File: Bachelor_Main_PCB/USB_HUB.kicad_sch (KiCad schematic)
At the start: 16 parts, among them J11 M20-9990245, U6 USB2514B-I/M2, Y3 SG-210STF 24Mhz

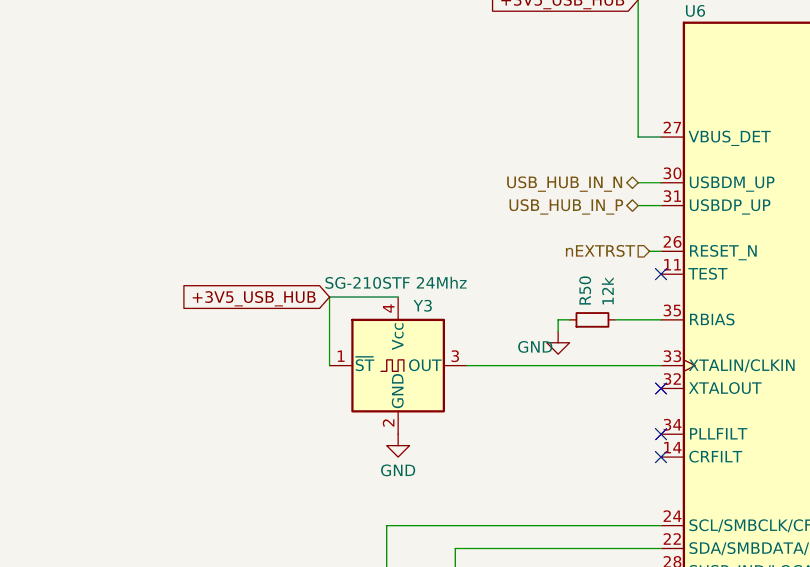
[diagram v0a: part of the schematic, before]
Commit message: Achematic review changes. Smal ones. Replaced TX_ON LED
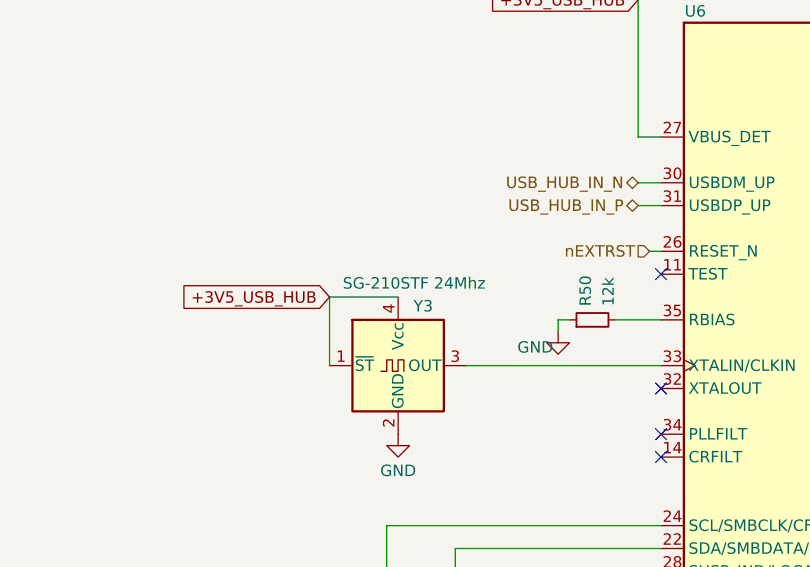
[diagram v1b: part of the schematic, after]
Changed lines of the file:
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@@
 		)
 		(property "Value" "SG-210STF 24Mhz"
-			(at 73.406 93.726 0)
+			(at 75.438 93.726 0)
 			(effects
 				(font

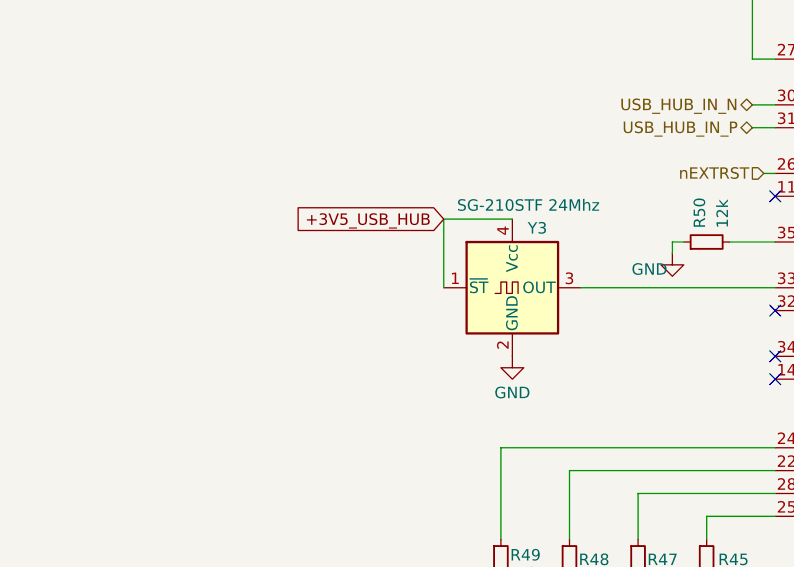
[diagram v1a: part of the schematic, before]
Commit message: added 100nF to 24Mhz oscillators
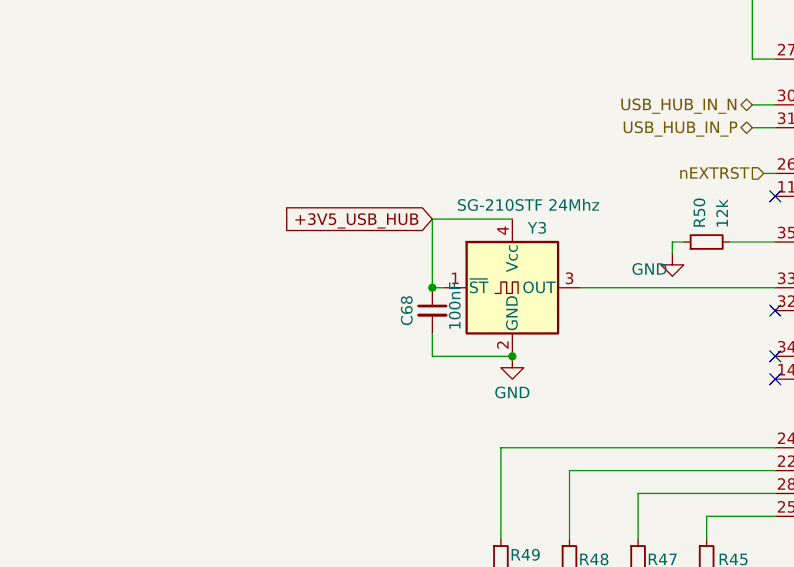
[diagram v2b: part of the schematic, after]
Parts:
- added C68: 100nF, Capacitor_SMD:C_0603_1608Metric, symbol Device:C_Small
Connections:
- net +3V5_USB_HUB: now also C68.1
- net GND: now also C68.2
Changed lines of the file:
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@@
+	)
+	(junction
+		(at 73.66 110.49)
+		(diameter 0)
+		(color 0 0 0 0)
 	)
 	(junction
@@
 	)
 	(junction
+		(at 64.77 102.87)
+		(diameter 0)
+		(color 0 0 0 0)
+	)
+	(junction
 		(at 148.59 182.88)
 		(diameter 0)
@@
 	(wire
 		(pts
+			(xy 64.77 110.49) (xy 73.66 110.49)
+		)
+		(stroke
+			(width 0)
+			(type default)
+		)
+	)
+	(wire
+		(pts
 			(xy 72.39 120.65) (xy 72.39 130.81)
 		)
@@
 	(wire
 		(pts
-			(xy 66.04 95.25) (xy 73.66 95.25)
+			(xy 64.77 95.25) (xy 73.66 95.25)
+		)
+		(stroke
+			(width 0)
+			(type default)
+		)
+	)
+	(wire
+		(pts
+			(xy 64.77 102.87) (xy 66.04 102.87)
 		)
 		(stroke
@@
 	(wire
 		(pts
-			(xy 66.04 102.87) (xy 66.04 95.25)
+			(xy 64.77 95.25) (xy 64.77 102.87)
 		)
 		(stroke
@@
 		(pts
 			(xy 133.35 182.88) (xy 140.97 182.88)
+		)
+		(stroke
+			(width 0)
+			(type default)
+		)
+	)
+	(wire
+		(pts
+			(xy 64.77 107.95) (xy 64.77 110.49)
 		)
 		(stroke
@@
 	(global_label "+3V5_USB_HUB"
 		(shape input)
-		(at 66.04 95.25 180)
+		(at 64.77 95.25 180)
 		(fields_autoplaced yes)
 		(effects
@@
 		)
 		(property "Intersheetrefs" "${INTERSHEET_REFS}"
-			(at 48.2986 95.25 0)
+			(at 47.0286 95.25 0)
 			(effects
 				(font
@@
 					(unit 1)
 				)
+			)
+		)
+	)
+	(symbol
+		(lib_id "Device:C_Small")
+		(at 64.77 105.41 0)
+		(unit 1)
+		(exclude_from_sim no)
+		(in_bom yes)
+		(on_board yes)
+		(dnp no)
+		(property "Reference" "C68"
+			(at 61.976 105.41 90)
+			(effects
+				(font
+					(size 1.27 1.27)
+				)
+			)
+		)
+		(property "Value" "100nF"
+			(at 67.31 104.902 90)
+			(effects
+				(font
+					(size 1.27 1.27)
+				)
+			)
+		)
+		(property "Footprint" "Capacitor_SMD:C_0603_1608Metric"
+			(at 64.77 105.41 0)
+			(effects
+				(font
+					(size 1.27 1.27)
+				)
+				(hide yes)
+			)
+		)
+		(property "Datasheet" "~"
+			(at 64.77 105.41 0)
+			(effects
+				(font
+					(size 1.27 1.27)
+				)
+				(hide yes)
+			)
+		)
+		(property "Description" "Unpolarized capacitor, small symbol"
+			(at 64.77 105.41 0)
+			(effects
+				(font
+					(size 1.27 1.27)
+				)
+				(hide yes)
+			)
+		)
+		(property "Field5" ""
+			(at 64.77 105.41 0)
+			(effects
+				(font
+					(size 1.27 1.27)
+				)
+				(hide yes)
+			)
+		)
+		(property "Field6" ""
+			(at 64.77 105.41 0)
+			(effects
+				(font
+					(size 1.27 1.27)
+				)
+				(hide yes)
+			)
+		)
+		(pin "2"
+		)
+		(pin "1"
+		)
+		(instances
+			(project "Bachelor_Main_PCB"
+				(path "/3544d663-329e-4884-b753-28436ca187e8/a2efe210-cbe4-4166-b2f4-897451b29d8a"
+					(reference "C68")
+					(unit 1)
+				)

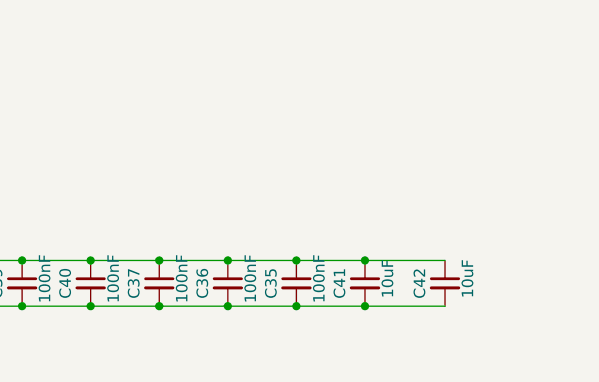
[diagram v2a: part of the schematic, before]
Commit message: Add correct 10uF partno
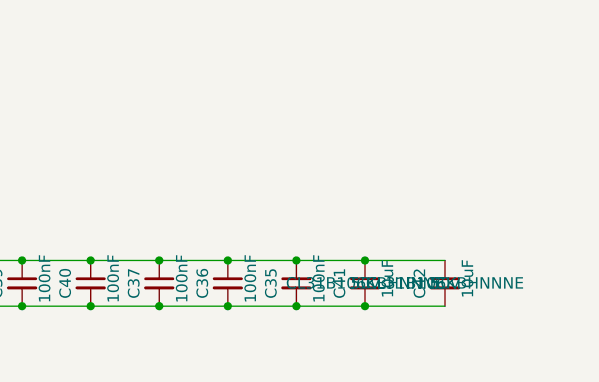
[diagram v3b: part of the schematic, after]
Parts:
- C41, C42: footprint Capacitor_SMD:C_0603_1608Metric -> Capacitor_SMD:C_1206_3216Metric; Part-no (none) -> CL31B106KBHNNNE; Voltage rating (none) -> 50v
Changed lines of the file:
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@@
 			)
 		)
-		(property "Footprint" "Capacitor_SMD:C_0603_1608Metric"
+		(property "Footprint" "Capacitor_SMD:C_1206_3216Metric"
 			(at 156.21 180.34 0)
 			(effects
@@
 				)
 				(hide yes)
+			)
+		)
+		(property "Part-no" "CL31B106KBHNNNE "
+			(at 156.21 180.34 0)
+			(effects
+				(font
+					(size 1.27 1.27)
+				)
+			)
+		)
+		(property "Voltage rating" "50v"
+			(at 156.21 180.34 0)
+			(effects
+				(font
+					(size 1.27 1.27)
+				)
 			)
 		)
@@
 			)
 		)
-		(property "Footprint" "Capacitor_SMD:C_0603_1608Metric"
+		(property "Footprint" "Capacitor_SMD:C_1206_3216Metric"
 			(at 165.1 180.34 0)
 			(effects
@@
 			)
 		)
+		(property "Part-no" "CL31B106KBHNNNE "
+			(at 165.1 180.34 0)
+			(effects
+				(font
+					(size 1.27 1.27)
+				)
+			)
+		)
+		(property "Voltage rating" "50v"
+			(at 165.1 180.34 0)
+			(effects
+				(font
+					(size 1.27 1.27)
+				)
+			)
+		)

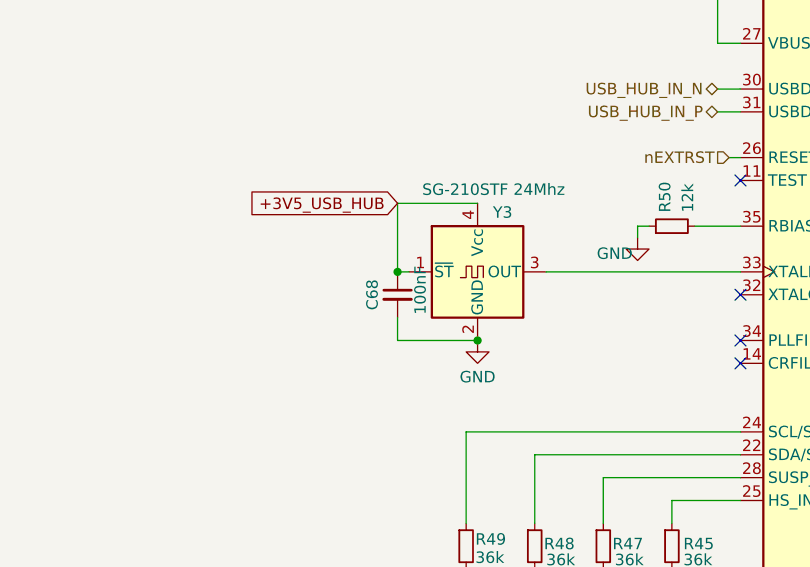
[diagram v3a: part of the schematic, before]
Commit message: Remove 24Mhz oscillators from hub and tranciever
Replaced with trace to PA8 pin which is the internaly supplied oscillator from the MCU
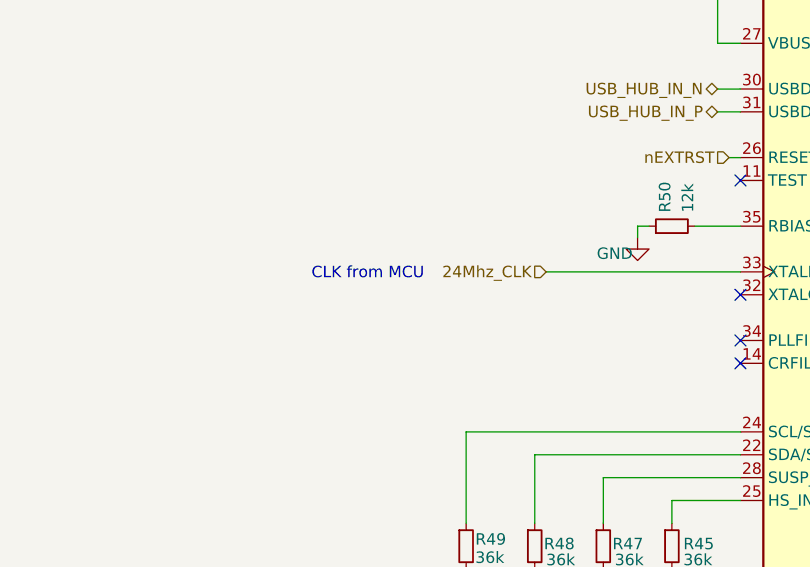
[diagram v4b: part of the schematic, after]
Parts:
- removed C68: 100nF, Capacitor_SMD:C_0603_1608Metric, symbol Device:C_Small
- removed Y3: SG-210STF 24Mhz, Oscillator:Oscillator_SMD_SeikoEpson_SG210-4Pin_2.5x2.0mm, symbol Oscillator:SG-210STF
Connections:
- net 24Mhz_CLK: now reaches U6.33 (XTALIN/CLKIN)
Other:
- note added: "CLK from MCU"

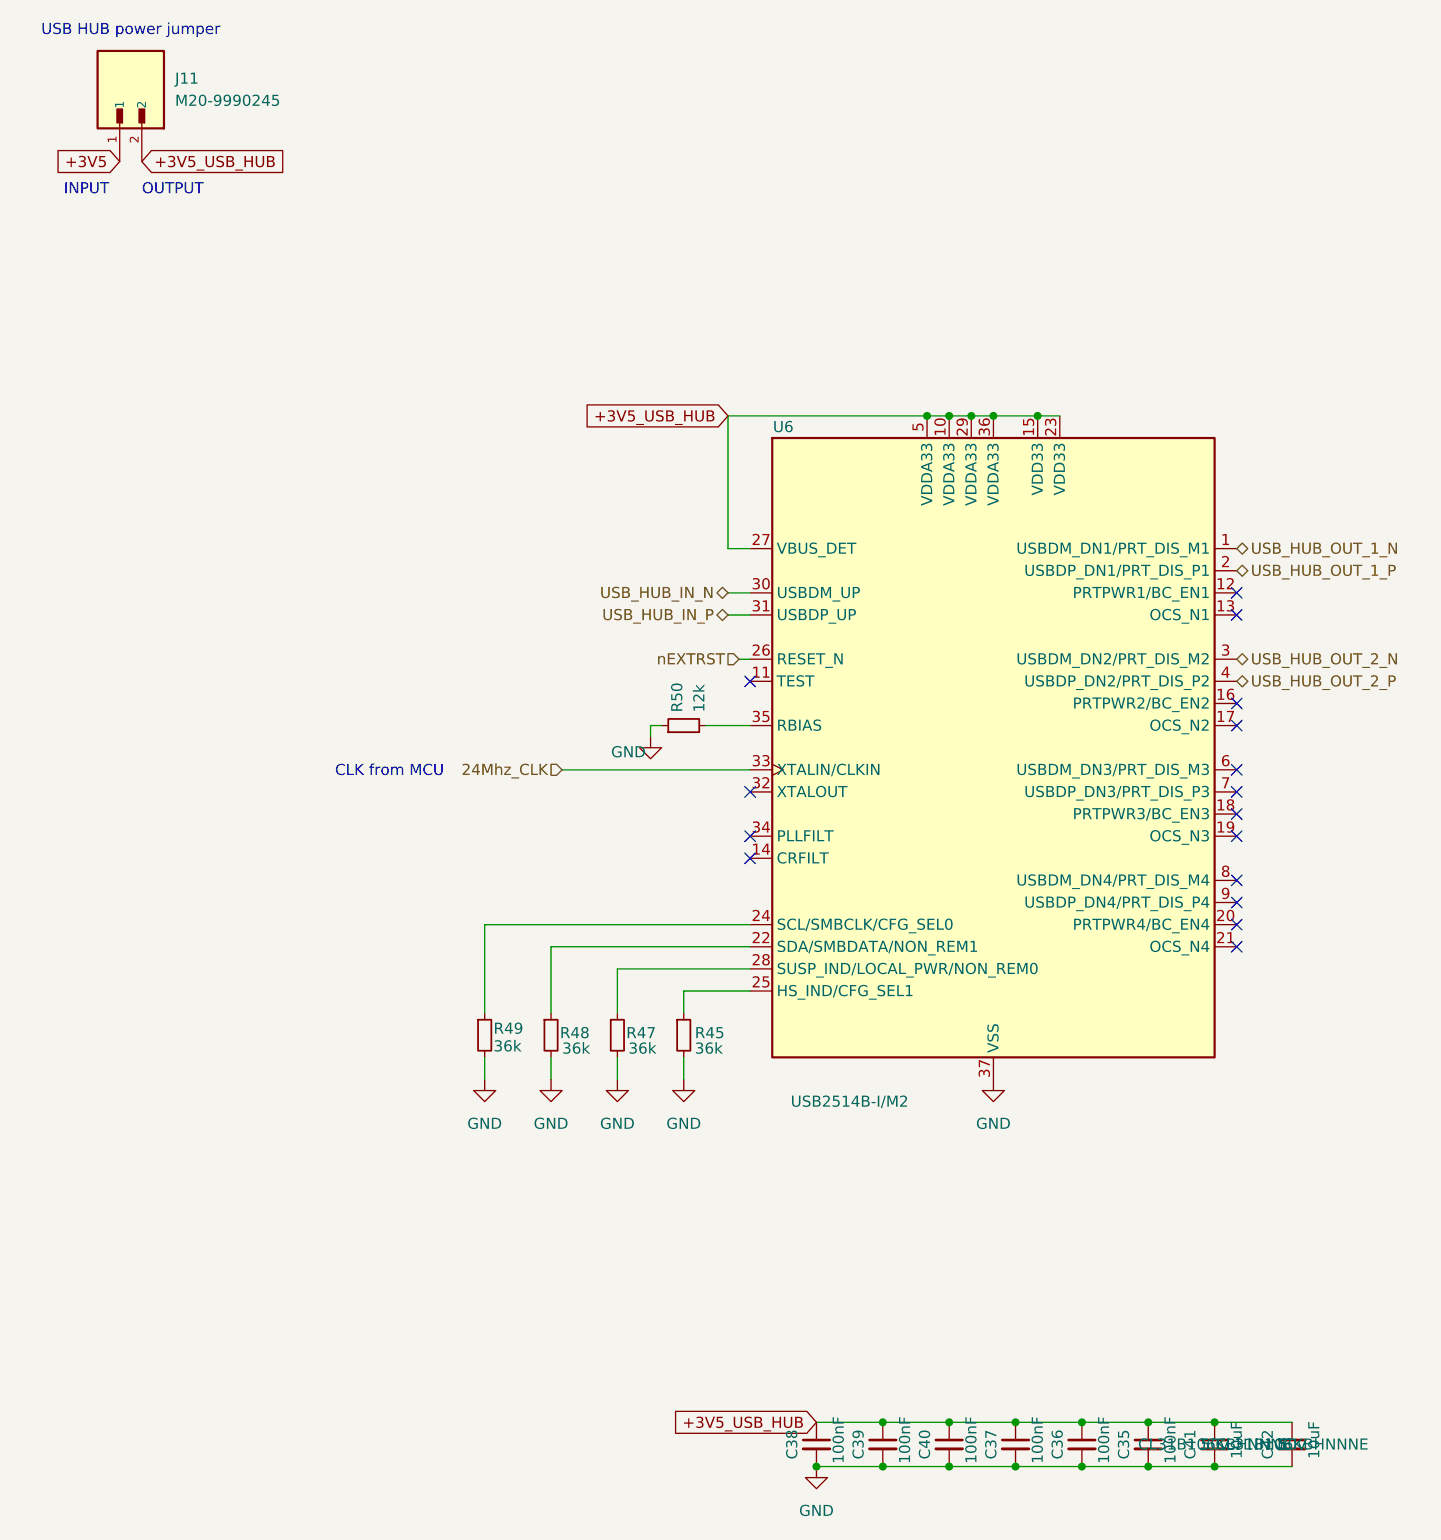
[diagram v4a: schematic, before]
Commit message: Updated the "Part-no" field in the symbol field table for all components
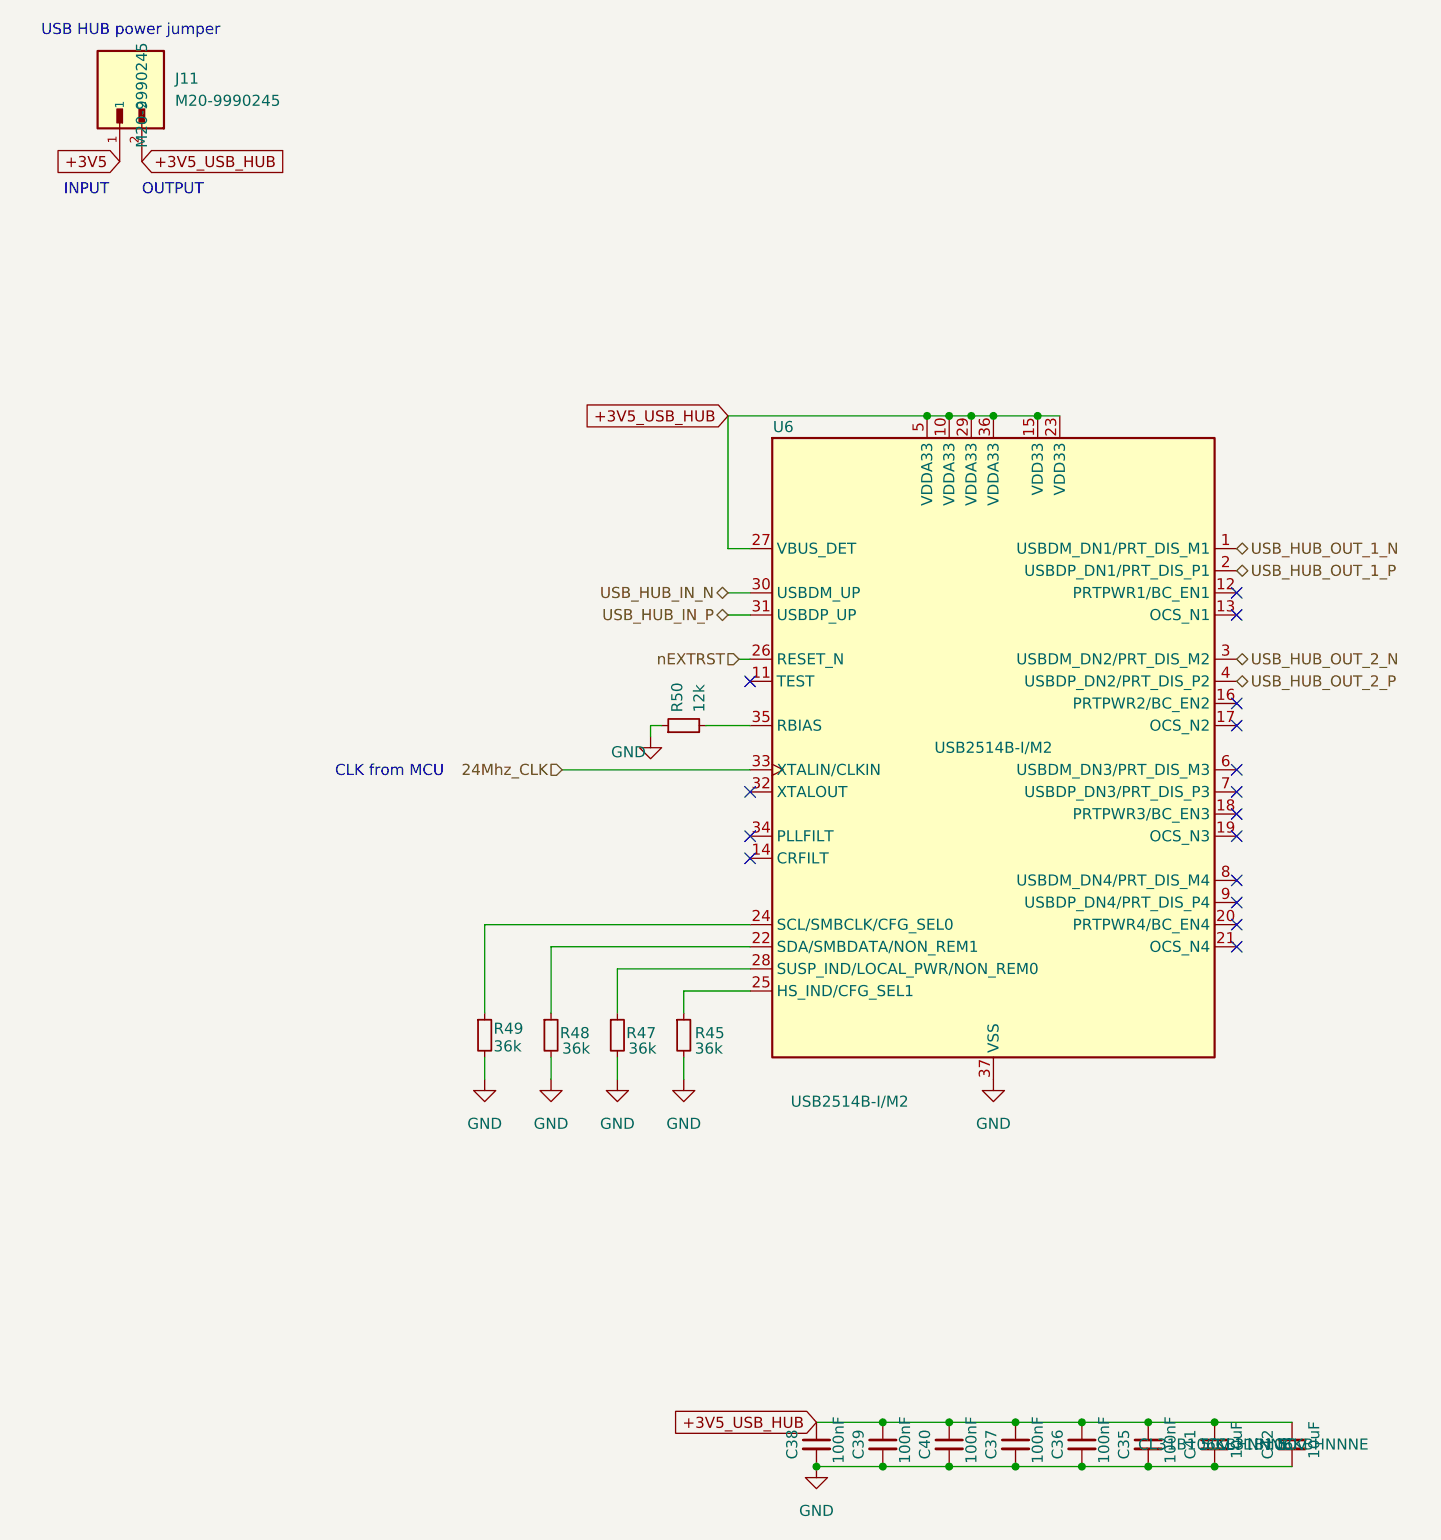
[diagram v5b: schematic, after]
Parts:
- J11: Part-no (none) -> M20-9990245
- U6: Part-no (none) -> USB2514B-I/M2
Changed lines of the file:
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@@
+			)
+		)
+		(property "Part-no" "USB2514B-I/M2"
+			(at 130.81 100.33 0)
+			(effects
+				(font
+					(size 1.27 1.27)
+				)
 			)
 		)
@@
 			)
 		)
+		(property "Part-no" "M20-9990245"
+			(at 33.02 25.4 0)
+			(effects
+				(font
+					(size 1.27 1.27)
+				)
+			)
+		)

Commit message: All resistors and capacitors correct footprints
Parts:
- R45, R47, R48, R49, R50: footprint Resistor_SMD:R_0402_1005Metric -> Resistor_SMD:R_0603_1608Metric
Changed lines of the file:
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@@
 			)
 		)
-		(property "Footprint" "Resistor_SMD:R_0402_1005Metric"
+		(property "Footprint" "Resistor_SMD:R_0603_1608Metric"
 			(at 72.39 133.35 0)
 			(effects
@@
 			)
 		)
-		(property "Footprint" "Resistor_SMD:R_0402_1005Metric"
+		(property "Footprint" "Resistor_SMD:R_0603_1608Metric"
 			(at 95.25 97.79 0)
 			(effects
@@
 			)
 		)
-		(property "Footprint" "Resistor_SMD:R_0402_1005Metric"
+		(property "Footprint" "Resistor_SMD:R_0603_1608Metric"
 			(at 80.01 133.35 0)
 			(effects
@@
 			)
 		)
-		(property "Footprint" "Resistor_SMD:R_0402_1005Metric"
+		(property "Footprint" "Resistor_SMD:R_0603_1608Metric"
 			(at 87.63 133.35 0)
 			(effects
@@
 			)
 		)
-		(property "Footprint" "Resistor_SMD:R_0402_1005Metric"
+		(property "Footprint" "Resistor_SMD:R_0603_1608Metric"
 			(at 95.25 133.35 0)
 			(effects
